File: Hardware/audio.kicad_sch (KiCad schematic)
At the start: 16 parts, among them J8 Conn_01x03, U4 LP5907MFX-3.3, U5 PCM5100

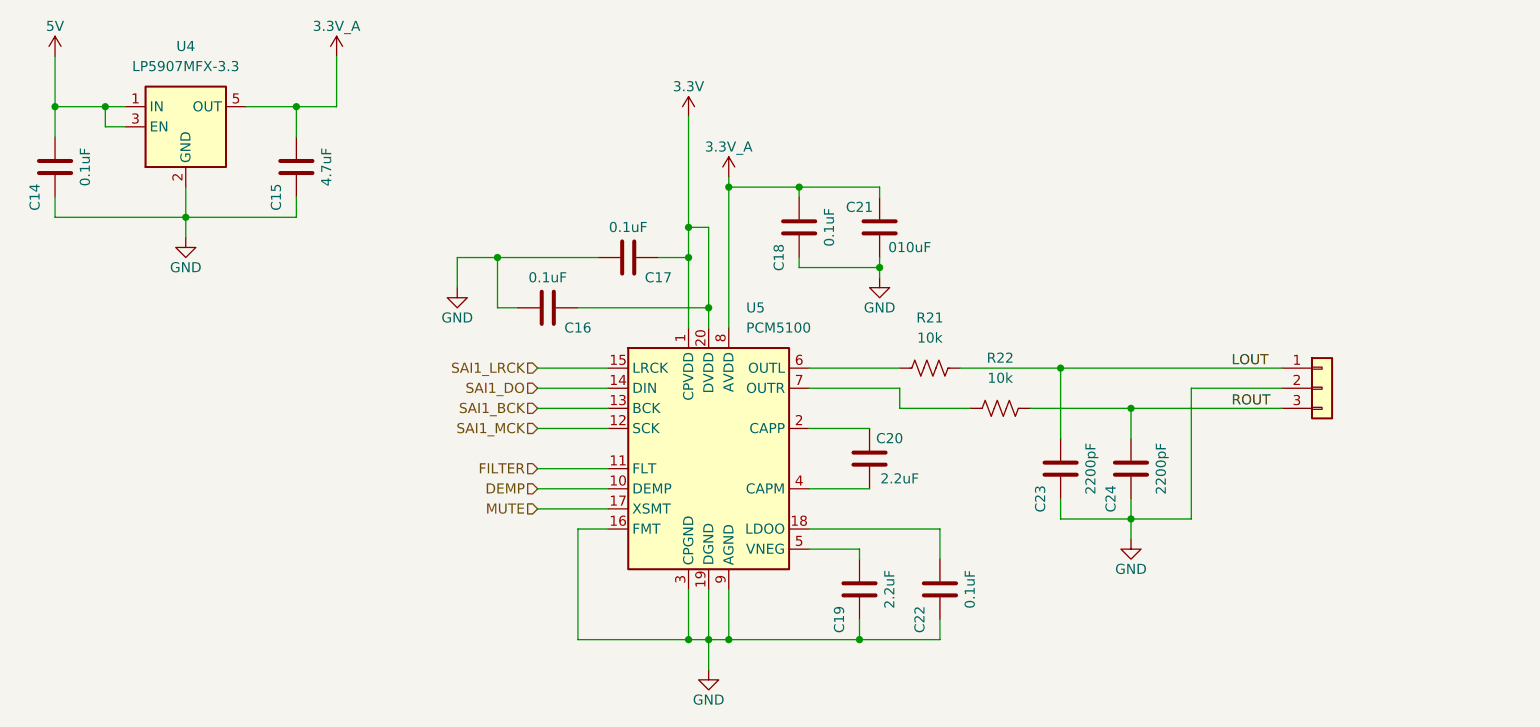
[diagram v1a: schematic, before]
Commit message: Update STM32 and power amp schematic.
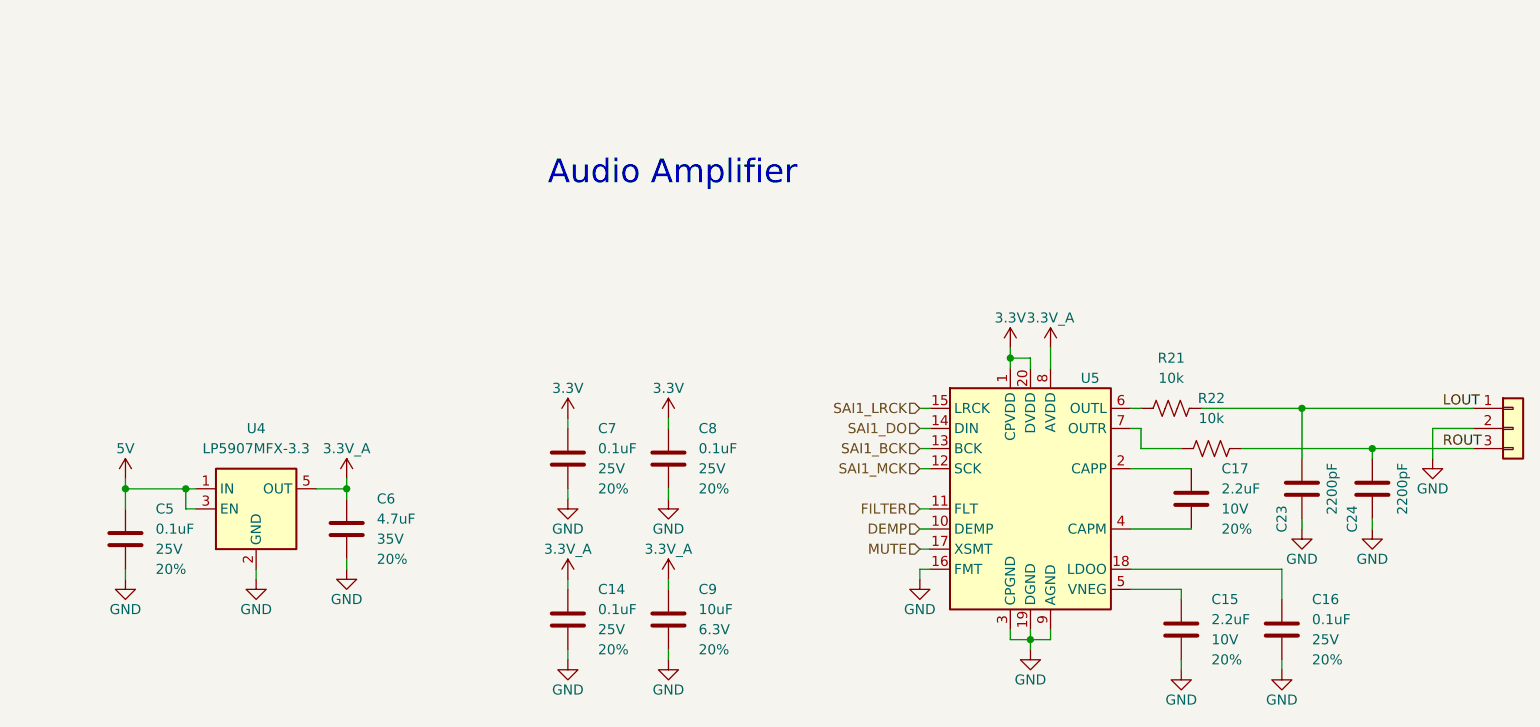
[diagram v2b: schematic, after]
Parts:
- removed C14, C16, C17, C18, C22: 0.1uF, SparkFun-Capacitor:C_0603_1608Metric, symbol Device:C
- removed C15: 4.7uF, SparkFun-Capacitor:C_0603_1608Metric, symbol Device:C
- removed C19, C20: 2.2uF, SparkFun-Capacitor:C_0603_1608Metric, symbol Device:C
- removed C21: 010uF, SparkFun-Capacitor:C_0603_1608Metric, symbol Device:C
- added C14, C16, C5, C7, C8: 0.1uF, SparkFun-Capacitor:C_0603_1608Metric, symbol SparkFun-Capacitor:0.1uF_0603_25V_20%
- added C15, C17: 2.2uF, SparkFun-Capacitor:C_0603_1608Metric, symbol SparkFun-Capacitor:2.2uF_0603_10V_20%
- added C6: 4.7uF, SparkFun-Capacitor:C_0603_1608Metric, symbol SparkFun-Capacitor:4.7uF_0603_35V_20%
- added C9: 10uF, SparkFun-Capacitor:C_0603_1608Metric, symbol SparkFun-Capacitor:10uF_0603_6.3V_20%
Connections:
- net 3.3V: now also C7.1, C8.1
- net 3.3V_A: now also C14.1, C6.1, C9.1
- net 5V: now also C5.1
- net GND: now also C14.2, C15.2, C16.2, C5.2, C6.2, C7.2, C8.2, C9.2
- net at U5.5 (VNEG): now also C15.1
- net at U5.2 (CAPP): now also C17.1
- net at U5.4 (CAPM): now also C17.2
- net at U5.18 (LDOO): now also C16.1
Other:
- note added: "Audio Amplifier"
- moved on the sheet: C23, C24, R21, R22, U4, U5

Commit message: Restored VBUS load switch / limit circuit and changed most of the passives to 0402s.
Signed-off-by: Jamie Robertson <jrr@robertsonics.com>
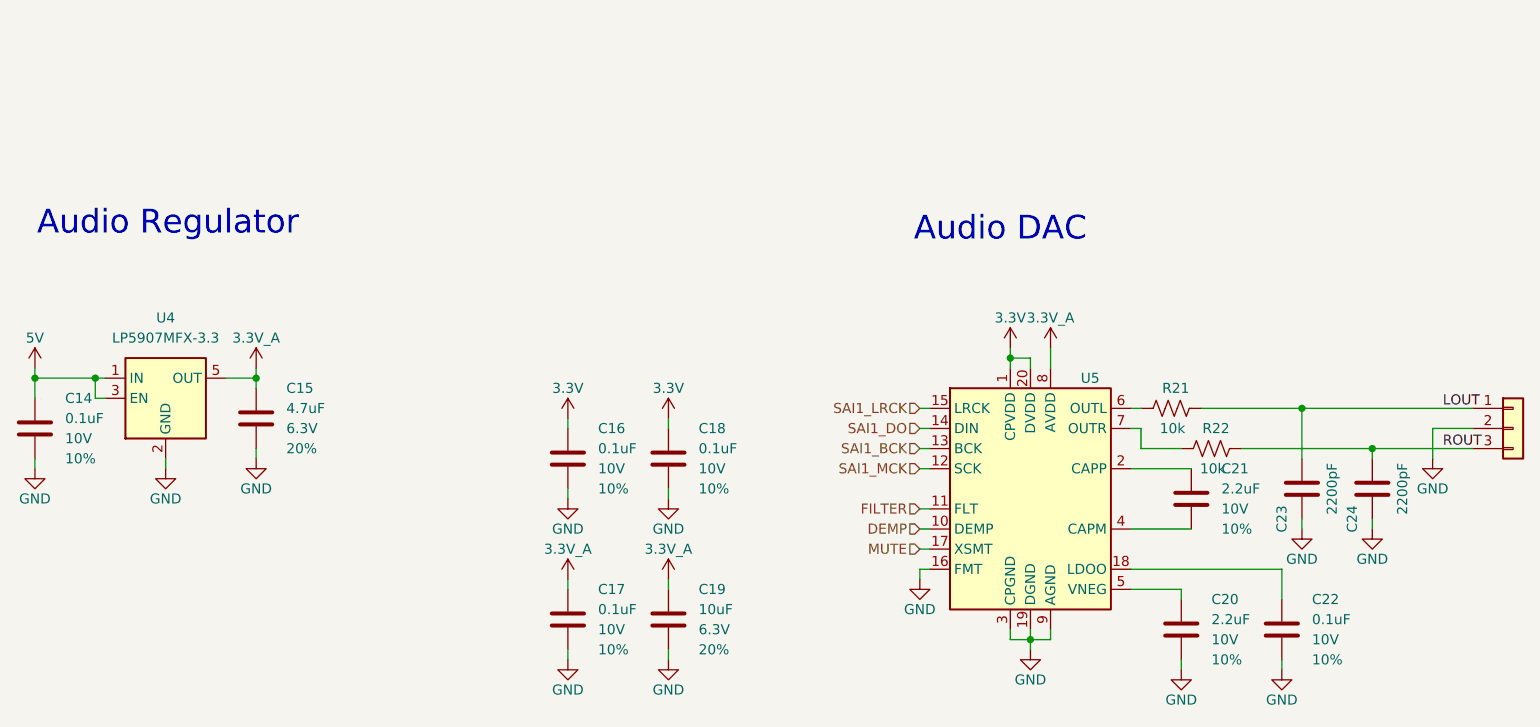
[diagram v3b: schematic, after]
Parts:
- removed C14, C16, C5, C7, C8: 0.1uF, SparkFun-Capacitor:C_0603_1608Metric, symbol SparkFun-Capacitor:0.1uF_0603_25V_20%
- removed C15, C17: 2.2uF, SparkFun-Capacitor:C_0603_1608Metric, symbol SparkFun-Capacitor:2.2uF_0603_10V_20%
- removed C6: 4.7uF, SparkFun-Capacitor:C_0603_1608Metric, symbol SparkFun-Capacitor:4.7uF_0603_35V_20%
- removed C9: 10uF, SparkFun-Capacitor:C_0603_1608Metric, symbol SparkFun-Capacitor:10uF_0603_6.3V_20%
- removed R21, R22: 10k, SparkFun-Resistor:R_0603_1608Metric, symbol SparkFun-Resistor:10k_0603
- added C14, C16, C17, C18, C22: 0.1uF, SparkFun-Capacitor:C_0402_1005Metric, symbol SparkFun-Capacitor:0.1uF_0402_10V_10%
- added C15: 4.7uF, SparkFun-Capacitor:C_0402_1005Metric, symbol SparkFun-Capacitor:4.7uF_0402_6.3V_10%
- added C19: 10uF, SparkFun-Capacitor:C_0402_1005Metric, symbol SparkFun-Capacitor:10uF_0402_6.3V_20%
- added C20, C21: 2.2uF, SparkFun-Capacitor:C_0402_1005Metric, symbol SparkFun-Capacitor:2.2uF_0402_10V_10%
- added R21, R22: 10k, SparkFun-Resistor:R_0402_1005Metric, symbol SparkFun-Resistor:10k_0402
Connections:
- net 3.3V: now also C16.1, C18.1
- net 3.3V_A: now also C15.1, C17.1, C19.1
- net 5V: now also C14.1
- net GND: now also C14.2, C15.2, C16.2, C17.2, C18.2, C19.2, C20.2, C22.2
- net LOUT: now also R21.1
- net ROUT: now also R22.1
- net at U5.7 (OUTR): now also R22.2
- net at U5.6 (OUTL): now also R21.2
- net at U5.5 (VNEG): now also C20.1
- net at U5.18 (LDOO): now also C22.1
- net at U5.2 (CAPP): now also C21.1
- net at U5.4 (CAPM): now also C21.2
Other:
- note added: "Audio DAC"
- note added: "Audio Regulator"
- note removed: "Audio Amplifier"
- moved on the sheet: U4

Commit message: Initial parts placement.
Signed-off-by: Jamie Robertson <jrr@robertsonics.com>
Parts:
- C23, C24: footprint SparkFun-Capacitor:C_0603_1608Metric -> SparkFun-Capacitor:C_0402_1005Metric
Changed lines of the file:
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@@
 			)
 		)
-		(property "Footprint" "SparkFun-Capacitor:C_0603_1608Metric"
+		(property "Footprint" "SparkFun-Capacitor:C_0402_1005Metric"
 			(at 222.5548 102.87 0)
 			(effects
@@
 			)
 		)
-		(property "Footprint" "SparkFun-Capacitor:C_0603_1608Metric"
+		(property "Footprint" "SparkFun-Capacitor:C_0402_1005Metric"
 			(at 213.6648 102.87 0)
 			(effects

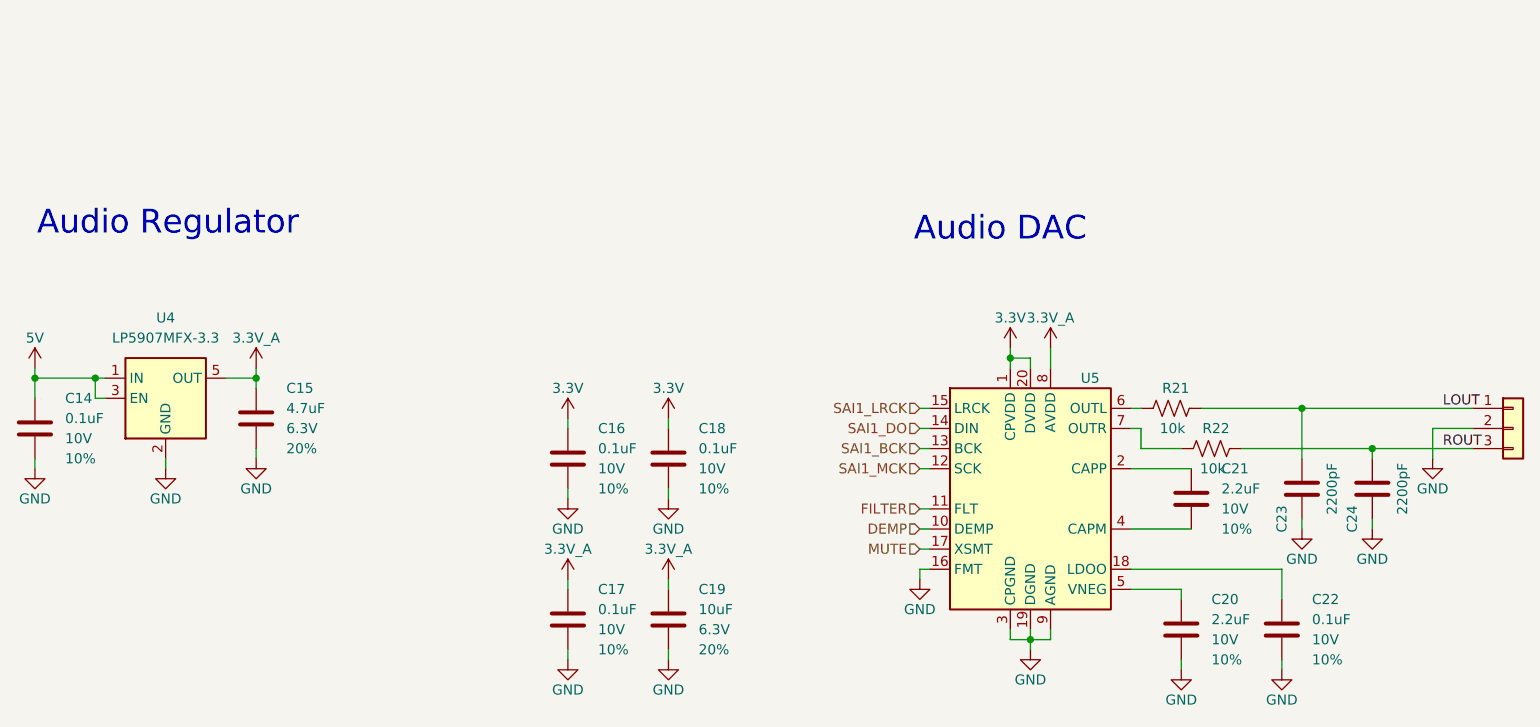
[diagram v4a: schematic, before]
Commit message: Update SCH to use new unique parts with PROD-IDs.
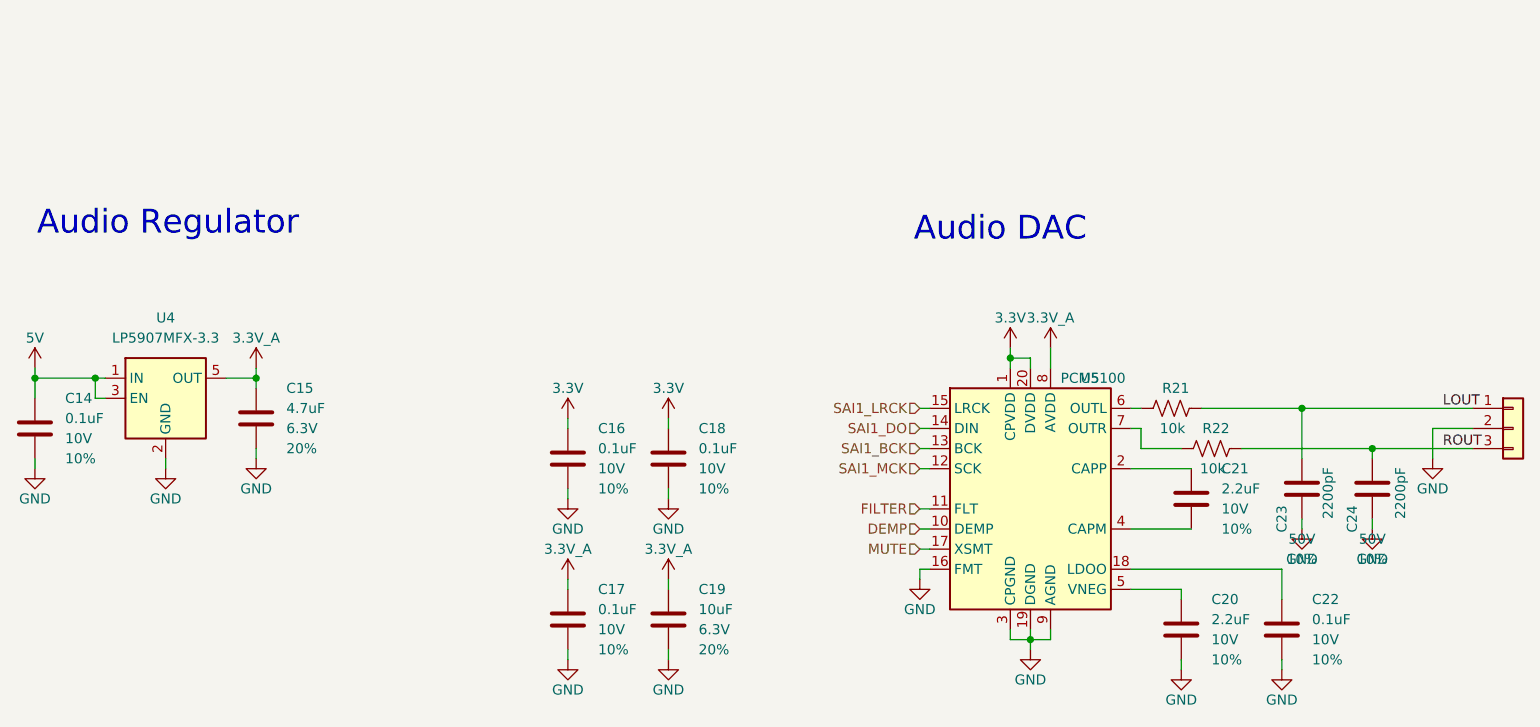
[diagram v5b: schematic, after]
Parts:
- C23, C24: symbol Device:C -> SparkFun-Capacitor:2200pF_0402_50V_10%; PROD_ID (none) -> CAP-22103; Tolerance (none) -> 10%; Voltage (none) -> 50V
- U4: footprint Package_TO_SOT_SMD:SOT-23-5 -> SparkFun-Semiconductor-Standard:SOT23-5; symbol Regulator_Linear:LP5907MFX-3.3 -> Qwiic_Turntable_Unique_Parts:LP5907MFX-3.3; PROD_ID (none) -> IC-22105
- U5: footprint Package_SO:TSSOP-20_4.4x6.5mm_P0.65mm -> SparkFun-Semiconductor-Standard:TSSOP-20_4.4x6.5mm_P0.65mm; symbol Audio:PCM5100 -> Qwiic_Turntable_Unique_Parts:PCM5100; PROD_ID (none) -> IC-11708
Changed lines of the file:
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@@
 	)
 	(symbol
-		(lib_id "Device:C")
+		(lib_id "SparkFun-Capacitor:2200pF_0402_50V_10%")
 		(at 223.52 99.06 0)
 		(mirror y)
@@
 		)
 		(property "Value" "2200pF"
-			(at 227.33 99.06 90)
-			(effects
-				(font
-					(size 1.27 1.27)
-				)
+			(at 227.076 102.87 90)
+			(effects
+				(font
+					(size 1.27 1.27)
+				)
+				(justify left)
 			)
 		)
 		(property "Footprint" "SparkFun-Capacitor:C_0402_1005Metric"
-			(at 222.5548 102.87 0)
-			(effects
-				(font
-					(size 1.27 1.27)
-				)
-				(hide yes)
-			)
-		)
-		(property "Datasheet" "~"
-			(at 223.52 99.06 0)
-			(effects
-				(font
-					(size 1.27 1.27)
-				)
-				(hide yes)
-			)
-		)
-		(property "Description" ""
-			(at 223.52 99.06 0)
-			(effects
-				(font
-					(size 1.27 1.27)
-				)
-				(hide yes)
+			(at 223.52 110.49 0)
+			(effects
+				(font
+					(size 1.27 1.27)
+				)
+				(hide yes)
+			)
+		)
+		(property "Datasheet" "https://cdn.sparkfun.com/assets/8/a/4/a/5/Kemet_Capacitor_Datasheet.pdf"
+			(at 223.52 115.57 0)
+			(effects
+				(font
+					(size 1.27 1.27)
+				)
+				(hide yes)
+			)
+		)
+		(property "Description" "Unpolarized capacitor"
+			(at 223.52 118.11 0)
+			(effects
+				(font
+					(size 1.27 1.27)
+				)
+				(hide yes)
+			)
+		)
+		(property "PROD_ID" "CAP-22103"
+			(at 223.52 113.03 0)
+			(effects
+				(font
+					(size 1.27 1.27)
+				)
+				(hide yes)
+			)
+		)
+		(property "Voltage" "50V"
+			(at 223.52 105.41 0)
+			(effects
+				(font
+					(size 1.27 1.27)
+				)
+			)
+		)
+		(property "Tolerance" "10%"
+			(at 223.52 107.95 0)
+			(effects
+				(font
+					(size 1.27 1.27)
+				)
 			)
 		)
@@
 	)
 	(symbol
-		(lib_id "Regulator_Linear:LP5907MFX-3.3")
+		(lib_id "Qwiic_Turntable_Unique_Parts:LP5907MFX-3.3")
 		(at 71.12 87.63 0)
 		(unit 1)
@@
 			)
 		)
-		(property "Footprint" "Package_TO_SOT_SMD:SOT-23-5"
-			(at 71.12 78.74 0)
+		(property "Footprint" "SparkFun-Semiconductor-Standard:SOT23-5"
+			(at 71.12 99.06 0)
 			(effects
 				(font
@@
 		)
 		(property "Datasheet" "http://www.ti.com/lit/ds/symlink/lp5907.pdf"
-			(at 71.12 74.93 0)
-			(effects
-				(font
-					(size 1.27 1.27)
-				)
-				(hide yes)
-			)
-		)
-		(property "Description" ""
-			(at 71.12 87.63 0)
+			(at 71.12 96.52 0)
+			(effects
+				(font
+					(size 1.27 1.27)
+				)
+				(hide yes)
+			)
+		)
+		(property "Description" "250mA Ultra-Low-Noise Low-IQ LDO, 3.3V, SOT-23"
+			(at 71.12 101.6 0)
+			(effects
+				(font
+					(size 1.27 1.27)
+				)
+				(hide yes)
+			)
+		)
+		(property "PROD_ID" "IC-22105"
+			(at 71.12 104.14 0)
 			(effects
 				(font
@@
 	)
 	(symbol
-		(lib_id "Device:C")
+		(lib_id "SparkFun-Capacitor:2200pF_0402_50V_10%")
 		(at 214.63 99.06 0)
 		(mirror y)
@@
 		)
 		(property "Value" "2200pF"
-			(at 218.44 99.06 90)
-			(effects
-				(font
-					(size 1.27 1.27)
-				)
+			(at 217.932 102.87 90)
+			(effects
+				(font
+					(size 1.27 1.27)
+				)
+				(justify left)
 			)
 		)
 		(property "Footprint" "SparkFun-Capacitor:C_0402_1005Metric"
-			(at 213.6648 102.87 0)
-			(effects
-				(font
-					(size 1.27 1.27)
-				)
-				(hide yes)
-			)
-		)
-		(property "Datasheet" "~"
-			(at 214.63 99.06 0)
-			(effects
-				(font
-					(size 1.27 1.27)
-				)
-				(hide yes)
-			)
-		)
-		(property "Description" ""
-			(at 214.63 99.06 0)
-			(effects
-				(font
-					(size 1.27 1.27)
-				)
-				(hide yes)
+			(at 214.63 110.49 0)
+			(effects
+				(font
+					(size 1.27 1.27)
+				)
+				(hide yes)
+			)
+		)
+		(property "Datasheet" "https://cdn.sparkfun.com/assets/8/a/4/a/5/Kemet_Capacitor_Datasheet.pdf"
+			(at 214.63 115.57 0)
+			(effects
+				(font
+					(size 1.27 1.27)
+				)
+				(hide yes)
+			)
+		)
+		(property "Description" "Unpolarized capacitor"
+			(at 214.63 118.11 0)
+			(effects
+				(font
+					(size 1.27 1.27)
+				)
+				(hide yes)
+			)
+		)
+		(property "PROD_ID" "CAP-22103"
+			(at 214.63 113.03 0)
+			(effects
+				(font
+					(size 1.27 1.27)
+				)
+				(hide yes)
+			)
+		)
+		(property "Voltage" "50V"
+			(at 214.63 105.41 0)
+			(effects
+				(font
+					(size 1.27 1.27)
+				)
+			)
+		)
+		(property "Tolerance" "10%"
+			(at 214.63 107.95 0)
+			(effects
+				(font
+					(size 1.27 1.27)
+				)
 			)
 		)
@@
 	)
 	(symbol
-		(lib_id "Audio:PCM5100")
+		(lib_id "Qwiic_Turntable_Unique_Parts:PCM5100")
 		(at 180.34 99.06 0)
 		(unit 1)
@@
 		)
 		(property "Value" "PCM5100"
-			(at 185.0741 83.82 0)
-			(effects
-				(font
-					(size 1.27 1.27)
-				)
-				(justify left)
-				(hide yes)
-			)
-		)
-		(property "Footprint" "Package_SO:TSSOP-20_4.4x6.5mm_P0.65mm"
-			(at 179.07 80.01 0)
+			(at 184.15 85.09 0)
+			(effects
+				(font
+					(size 1.27 1.27)
+				)
+				(justify left)
+			)
+		)
+		(property "Footprint" "SparkFun-Semiconductor-Standard:TSSOP-20_4.4x6.5mm_P0.65mm"
+			(at 180.34 121.92 0)
 			(effects
 				(font
@@
 		)
 		(property "Datasheet" "http://www.ti.com/lit/ds/symlink/pcm5100.pdf"
-			(at 179.07 80.01 0)
-			(effects
-				(font
-					(size 1.27 1.27)
-				)
-				(hide yes)
-			)
-		)
-		(property "Description" ""
-			(at 180.34 99.06 0)
-			(effects
-				(font
+			(at 180.34 119.38 0)
+			(effects
+				(font
+					(size 1.27 1.27)
+				)
+				(hide yes)
+			)
+		)
+		(property "Description" "2VRMS DirectPath, 100dB Audio Stereo DAC with 32-bit, 384kHz PCM Interface, TSSOP-20"
+			(at 180.34 124.46 0)
+			(effects
+				(font
+					(size 1.27 1.27)
+				)
+				(hide yes)
+			)
+		)
+		(property "PROD_ID" "IC-11708"
+			(at 180.34 127 0)
+			(effects
+				(font
